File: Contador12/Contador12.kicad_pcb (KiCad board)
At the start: 2 copper layers, 43.2 x 38.8 mm, 13 parts, among them J1 Conector_ESP, U2 ESP-12E

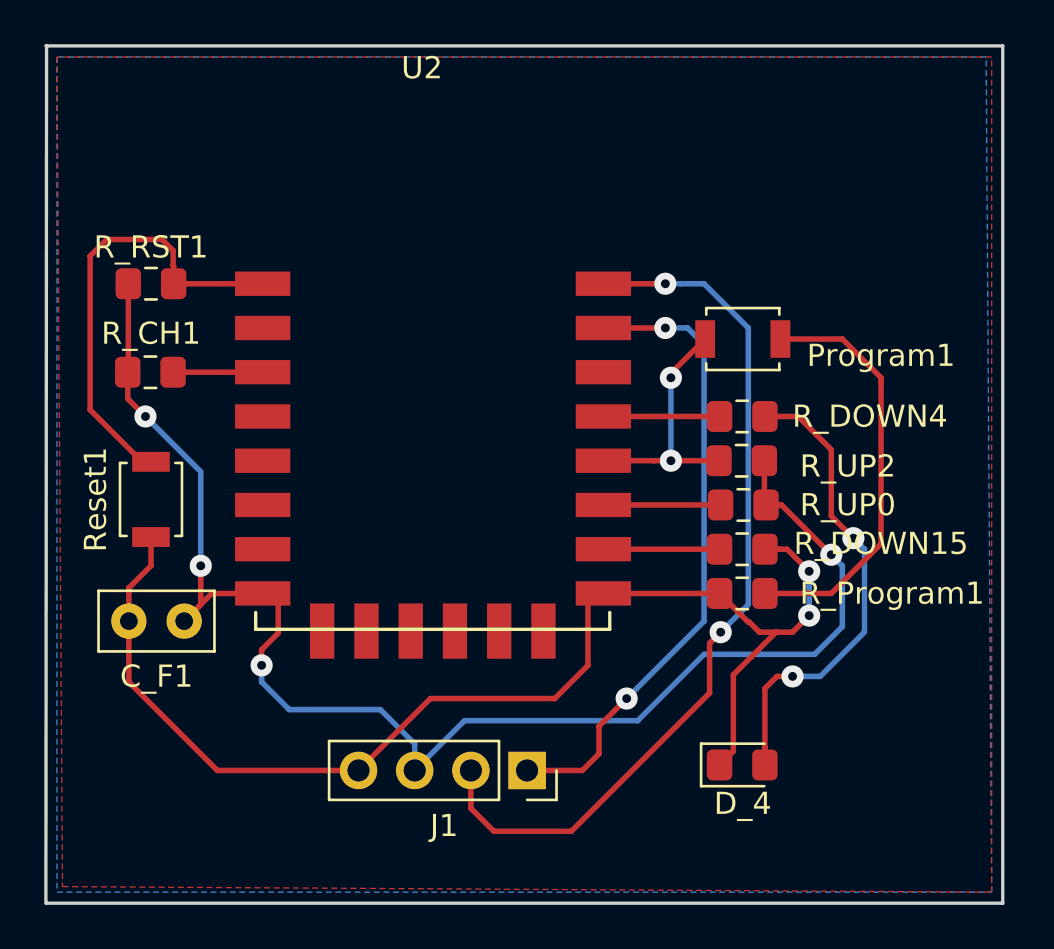
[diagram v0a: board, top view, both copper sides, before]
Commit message: Serigrafia y agujeros agregados
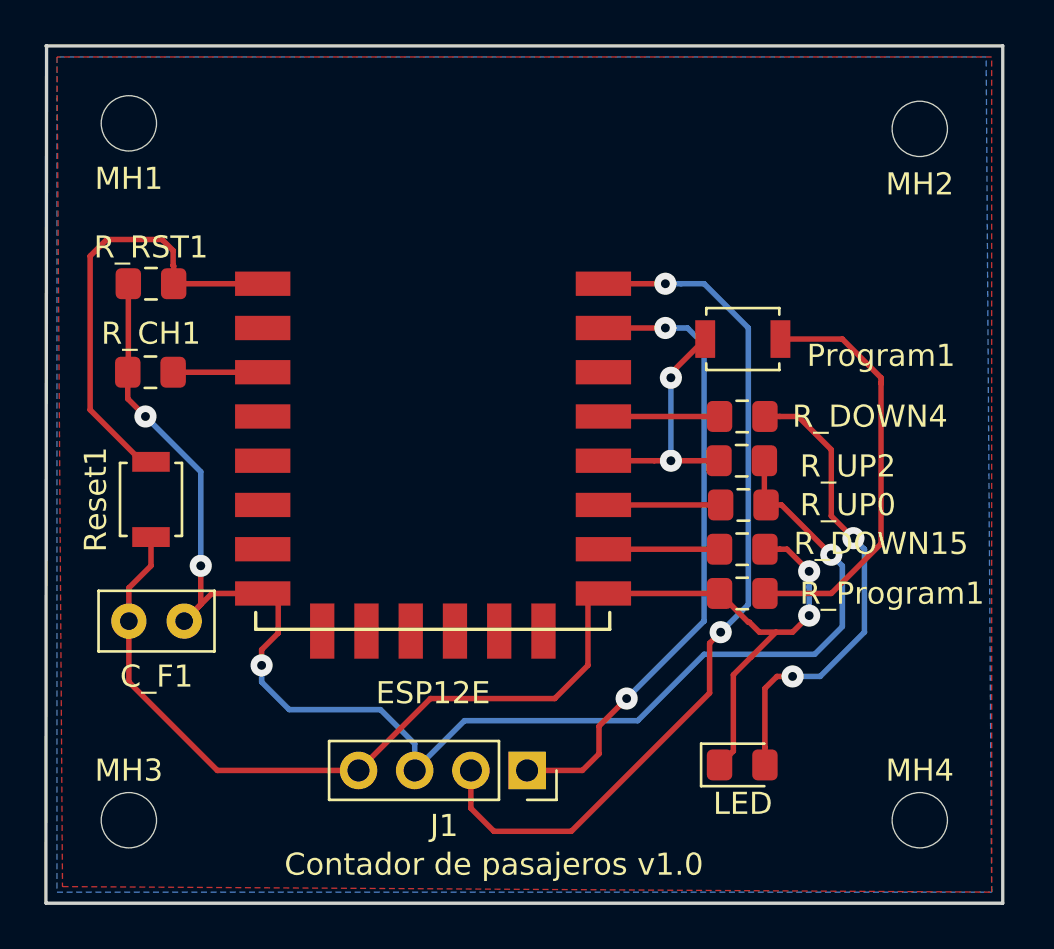
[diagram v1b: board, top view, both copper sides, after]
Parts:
- added MH1: MountingHole, Mounting_Holes:MountingHole_2.5mm, F.Cu at (180.2, 27.8)
- added MH2: MountingHole, Mounting_Holes:MountingHole_2.5mm, F.Cu at (216.0, 28.0)
- added MH3: MountingHole, Mounting_Holes:MountingHole_2.5mm, F.Cu at (180.2, 59.2)
- added MH4: MountingHole, Mounting_Holes:MountingHole_2.5mm, F.Cu at (216.0, 59.2)
- renumbered U2 to ESP12E, D_4 to LED
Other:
- board text added: "Contador de pasajeros v1.0"
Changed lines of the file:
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@@
   (general
     (thickness 1.6)
-    (drawings 4)
+    (drawings 5)
     (tracks 130)
     (zones 0)
-    (modules 13)
+    (modules 17)
     (nets 25)
   )
@@
     (tags "LED handsolder")
     (attr smd)
-    (fp_text reference D_4 (at 0.025 1.75) (layer F.SilkS)
+    (fp_text reference LED (at 0.025 1.75) (layer F.SilkS)
       (effects (font (size 1 1) (thickness 0.15)))
     )
@@
     (descr "Module, ESP-8266, ESP-12, 16 pad, SMD")
     (tags "Module ESP-8266 ESP8266")
-    (fp_text reference U2 (at 6.5 -9.75 180) (layer F.SilkS)
+    (fp_text reference ESP12E (at 7 18.5 180) (layer F.SilkS)
       (effects (font (size 1 1) (thickness 0.15)))
     )
@@
     )
   )
+  (module Mounting_Holes:MountingHole_2.5mm (layer F.Cu)
+    (at 180.25 27.75)
+    (descr "Mounting Hole 2.5mm, no annular")
+    (tags "mounting hole 2.5mm no annular")
+    (attr virtual)
+    (fp_text reference MH1 (at 0 2.5) (layer F.SilkS)
+      (effects (font (size 1 1) (thickness 0.15)))
+    )
+    (fp_text value MountingHole (at 7.5 -2) (layer F.Fab)
+      (effects (font (size 1 1) (thickness 0.15)))
+    )
+    (fp_text user %R (at 0.3 0) (layer F.Fab)
+      (effects (font (size 1 1) (thickness 0.15)))
+    )
+    (fp_circle (center 0 0) (end 2.5 0) (layer Cmts.User) (width 0.15))
+    (fp_circle (center 0 0) (end 2.75 0) (layer F.CrtYd) (width 0.05))
+    (pad 1 np_thru_hole circle (at 0 0) (size 2.5 2.5) (drill 2.5) (layers *.Cu *.Mask))
+  )
+  (module Mounting_Holes:MountingHole_2.5mm (layer F.Cu)
+    (at 216 28)
+    (descr "Mounting Hole 2.5mm, no annular")
+    (tags "mounting hole 2.5mm no annular")
+    (attr virtual)
+    (fp_text reference MH2 (at 0 2.5) (layer F.SilkS)
+      (effects (font (size 1 1) (thickness 0.15)))
+    )
+    (fp_text value MountingHole (at -7.25 -2.25) (layer F.Fab)
+      (effects (font (size 1 1) (thickness 0.15)))
+    )
+    (fp_text user %R (at 0.3 0) (layer F.Fab)
+      (effects (font (size 1 1) (thickness 0.15)))
+    )
+    (fp_circle (center 0 0) (end 2.5 0) (layer Cmts.User) (width 0.15))
+    (fp_circle (center 0 0) (end 2.75 0) (layer F.CrtYd) (width 0.05))
+    (pad 1 np_thru_hole circle (at 0 0) (size 2.5 2.5) (drill 2.5) (layers *.Cu *.Mask))
+  )
+  (module Mounting_Holes:MountingHole_2.5mm (layer F.Cu)
+    (at 180.25 59.25)
+    (descr "Mounting Hole 2.5mm, no annular")
+    (tags "mounting hole 2.5mm no annular")
+    (attr virtual)
+    (fp_text reference MH3 (at 0 -2.25) (layer F.SilkS)
+      (effects (font (size 1 1) (thickness 0.15)))
+    )
+    (fp_text value MountingHole (at 1.75 -3.75) (layer F.Fab)
+      (effects (font (size 1 1) (thickness 0.15)))
+    )
+    (fp_circle (center 0 0) (end 2.75 0) (layer F.CrtYd) (width 0.05))
+    (fp_circle (center 0 0) (end 2.5 0) (layer Cmts.User) (width 0.15))
+    (fp_text user %R (at 0.3 0) (layer F.Fab)
+      (effects (font (size 1 1) (thickness 0.15)))
+    )
+    (pad 1 np_thru_hole circle (at 0 0) (size 2.5 2.5) (drill 2.5) (layers *.Cu *.Mask))
+  )
+  (module Mounting_Holes:MountingHole_2.5mm (layer F.Cu)
+    (at 216 59.25)
+    (descr "Mounting Hole 2.5mm, no annular")
+    (tags "mounting hole 2.5mm no annular")
+    (attr virtual)
+    (fp_text reference MH4 (at 0 -2.25) (layer F.SilkS)
+      (effects (font (size 1 1) (thickness 0.15)))
+    )
+    (fp_text value MountingHole (at -1.5 -0.25) (layer F.Fab)
+      (effects (font (size 1 1) (thickness 0.15)))
+    )
+    (fp_circle (center 0 0) (end 2.75 0) (layer F.CrtYd) (width 0.05))
+    (fp_circle (center 0 0) (end 2.5 0) (layer Cmts.User) (width 0.15))
+    (fp_text user %R (at 0.3 0) (layer F.Fab)
+      (effects (font (size 1 1) (thickness 0.15)))
+    )
+    (pad 1 np_thru_hole circle (at 0 0) (size 2.5 2.5) (drill 2.5) (layers *.Cu *.Mask))
+  )
+  (gr_text "Contador de pasajeros v1.0" (at 196.75 61.25) (layer F.SilkS)
+    (effects (font (size 1 1) (thickness 0.25)))
+  )
   (gr_line (start 219.75 24.25) (end 176.5 24.25) (layer Edge.Cuts) (width 0.15))

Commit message: Correcciones adrian
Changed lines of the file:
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@@
     (thickness 1.6)
     (drawings 5)
-    (tracks 130)
+    (tracks 133)
     (zones 0)
     (modules 17)
@@
   (page A4)
   (layers
-    (0 F.Cu signal hide)
-    (31 B.Cu signal)
+    (0 F.Cu signal)
+    (31 B.Cu signal hide)
     (32 B.Adhes user)
     (33 F.Adhes user)
@@
     (tags "Tactile Switch")
     (attr smd)
-    (fp_text reference Program1 (at 6.25 0.75 180) (layer F.SilkS)
+    (fp_text reference Program1 (at 6.25 0 180) (layer F.SilkS)
       (effects (font (size 1 1) (thickness 0.15)))
     )
@@
       (effects (font (size 1 1) (thickness 0.15)))
     )
-    (fp_text user %R (at 6.25 0.75 180) (layer F.Fab)
+    (fp_text user %R (at 6.25 0 180) (layer F.Fab)
       (effects (font (size 1 1) (thickness 0.15)))
     )
@@
     (tags "Tactile Switch")
     (attr smd)
-    (fp_text reference Reset1 (at 0 2.5 270) (layer F.SilkS)
+    (fp_text reference Reset1 (at -3 0) (layer F.SilkS)
       (effects (font (size 1 1) (thickness 0.15)))
     )
@@
     (fp_line (start 2.4 1.65) (end 2.4 -1.65) (layer F.CrtYd) (width 0.05))
     (fp_line (start -2.4 1.65) (end 2.4 1.65) (layer F.CrtYd) (width 0.05))
-    (fp_text user %R (at 0 2.5 270) (layer F.Fab)
+    (fp_text user %R (at -3 0) (layer F.Fab)
       (effects (font (size 1 1) (thickness 0.15)))
     )
@@
     (tags "mounting hole 2.5mm no annular")
     (attr virtual)
-    (fp_text reference MH1 (at 0 2.5) (layer F.SilkS)
-      (effects (font (size 1 1) (thickness 0.15)))
-    )
-    (fp_text value MountingHole (at 7.5 -2) (layer F.Fab)
+    (fp_text reference MH1 (at 0 2.5) (layer F.SilkS) hide
+      (effects (font (size 1 1) (thickness 0.15)))
+    )
+    (fp_text value MountingHole (at 7.5 -2) (layer F.Fab) hide
       (effects (font (size 1 1) (thickness 0.15)))
     )
@@
     (tags "mounting hole 2.5mm no annular")
     (attr virtual)
-    (fp_text reference MH2 (at 0 2.5) (layer F.SilkS)
-      (effects (font (size 1 1) (thickness 0.15)))
-    )
-    (fp_text value MountingHole (at -7.25 -2.25) (layer F.Fab)
+    (fp_text reference MH2 (at 0 2.5) (layer F.SilkS) hide
+      (effects (font (size 1 1) (thickness 0.15)))
+    )
+    (fp_text value MountingHole (at -7.25 -2.25) (layer F.Fab) hide
       (effects (font (size 1 1) (thickness 0.15)))
     )
@@
     (tags "mounting hole 2.5mm no annular")
     (attr virtual)
-    (fp_text reference MH3 (at 0 -2.25) (layer F.SilkS)
-      (effects (font (size 1 1) (thickness 0.15)))
-    )
-    (fp_text value MountingHole (at 1.75 -3.75) (layer F.Fab)
+    (fp_text reference MH3 (at 0 -2.25) (layer F.SilkS) hide
+      (effects (font (size 1 1) (thickness 0.15)))
+    )
+    (fp_text value MountingHole (at 1.75 -3.75) (layer F.Fab) hide
       (effects (font (size 1 1) (thickness 0.15)))
     )
@@
     (tags "mounting hole 2.5mm no annular")
     (attr virtual)
-    (fp_text reference MH4 (at 0 -2.25) (layer F.SilkS)
-      (effects (font (size 1 1) (thickness 0.15)))
-    )
-    (fp_text value MountingHole (at -1.5 -0.25) (layer F.Fab)
+    (fp_text reference MH4 (at 0 -2.25) (layer F.SilkS) hide
+      (effects (font (size 1 1) (thickness 0.15)))
+    )
+    (fp_text value MountingHole (at -1.5 -0.25) (layer F.Fab) hide
       (effects (font (size 1 1) (thickness 0.15)))
     )
@@
   (segment (start 211.25 51.75) (end 206.25 51.75) (width 0.25) (layer B.Cu) (net 3))
   (segment (start 206.25 51.75) (end 203.25 54.75) (width 0.25) (layer B.Cu) (net 3))
-  (segment (start 195.42 54.75) (end 193.17 57) (width 0.25) (layer B.Cu) (net 3))
   (segment (start 203.25 54.75) (end 195.42 54.75) (width 0.25) (layer B.Cu) (net 3))
   (segment (start 180.225 38.975) (end 180.2 39) (width 0.25) (layer F.Cu) (net 3))
@@
   (segment (start 184 49) (end 182.75 50.25) (width 0.25) (layer F.Cu) (net 3))
   (segment (start 187 49) (end 184 49) (width 0.25) (layer F.Cu) (net 3))
-  (segment (start 193.17 55.797919) (end 191.622081 54.25) (width 0.25) (layer B.Cu) (net 3))
-  (segment (start 193.17 57) (end 193.17 55.797919) (width 0.25) (layer B.Cu) (net 3))
   (segment (start 191.622081 54.25) (end 187.5 54.25) (width 0.25) (layer B.Cu) (net 3))
   (via (at 186.25 52.25) (size 1) (drill 0.4) (layers F.Cu B.Cu) (net 3))
@@
   (segment (start 186.25 51.542894) (end 187 50.792894) (width 0.25) (layer F.Cu) (net 3))
   (segment (start 186.25 52.25) (end 186.25 51.542894) (width 0.25) (layer F.Cu) (net 3))
+  (segment (start 194.92 54.25) (end 195.42 54.75) (width 0.25) (layer B.Cu) (net 3))
+  (segment (start 193.5 54.25) (end 194.92 54.25) (width 0.25) (layer B.Cu) (net 3))
+  (segment (start 193.17 54.33) (end 193.25 54.25) (width 0.25) (layer B.Cu) (net 3))
+  (segment (start 193.17 57) (end 193.17 54.33) (width 0.25) (layer B.Cu) (net 3))
+  (segment (start 191.622081 54.25) (end 193.25 54.25) (width 0.25) (layer B.Cu) (net 3))
+  (segment (start 193.25 54.25) (end 193.5 54.25) (width 0.25) (layer B.Cu) (net 3))
   (via (at 204.5 35) (size 1) (drill 0.4) (layers F.Cu B.Cu) (net 4))
   (segment (start 201 35) (end 204.5 35) (width 0.25) (layer F.Cu) (net 4))
@@
     (polygon
       (pts
-        (xy 177 24.75) (xy 177 62.5) (xy 219.25 62.5) (xy 219 24.75)
+        (xy 177 24.75) (xy 177 62.5) (xy 219.25 62.5) (xy 219.25 24.75)
       )
     )
